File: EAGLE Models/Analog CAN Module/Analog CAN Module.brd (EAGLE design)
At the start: 98.3 x 80 mm, 230 parts, among them IC1 AT90CAN128, IC2 MCP2551SO8, IC3 NUP2105L, IC5 FT232RL, Q1 56P2859, U1 LTC2053, U10 LTC2053, U11 LTC2053, U12 LTC2053, U13 LTC2053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

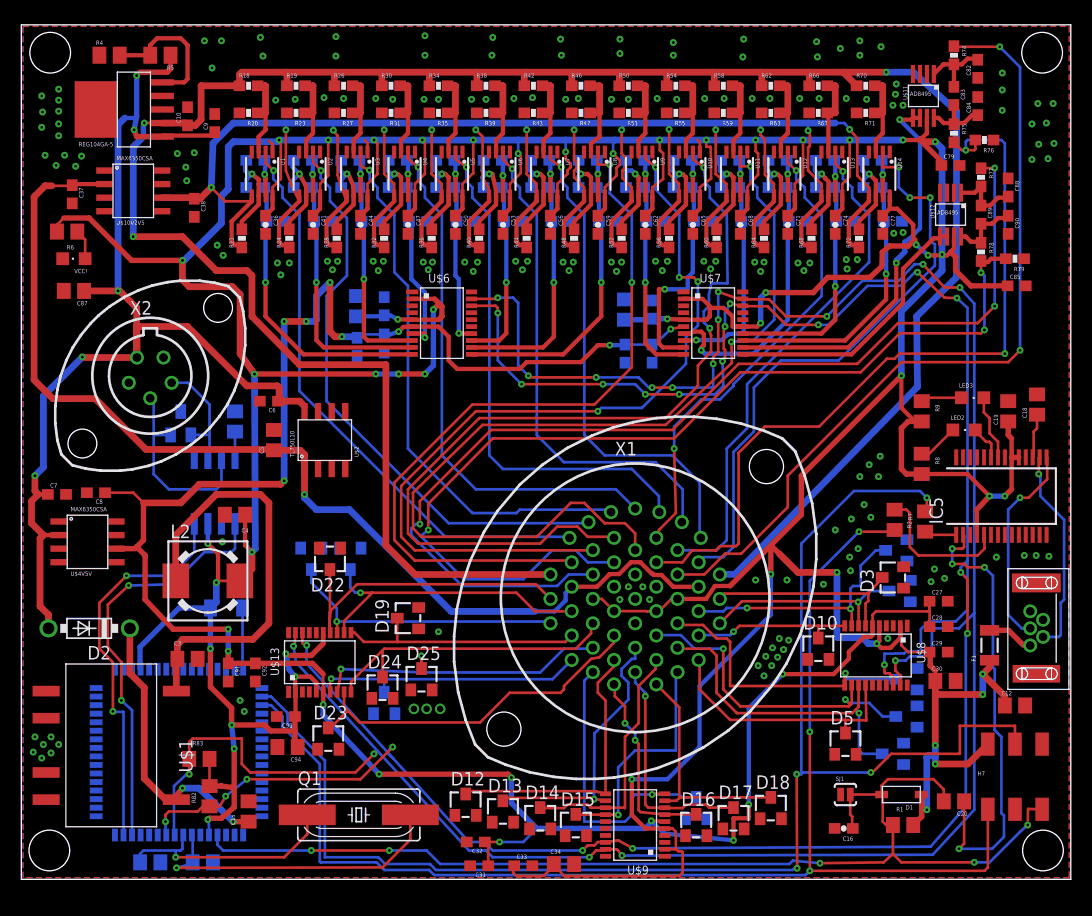
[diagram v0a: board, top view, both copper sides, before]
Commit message: Added USB connector and FTDI Chip, fixed feedback according to daniel, added PTC fuse, Added schottky diode for RVP and battery reverse bias
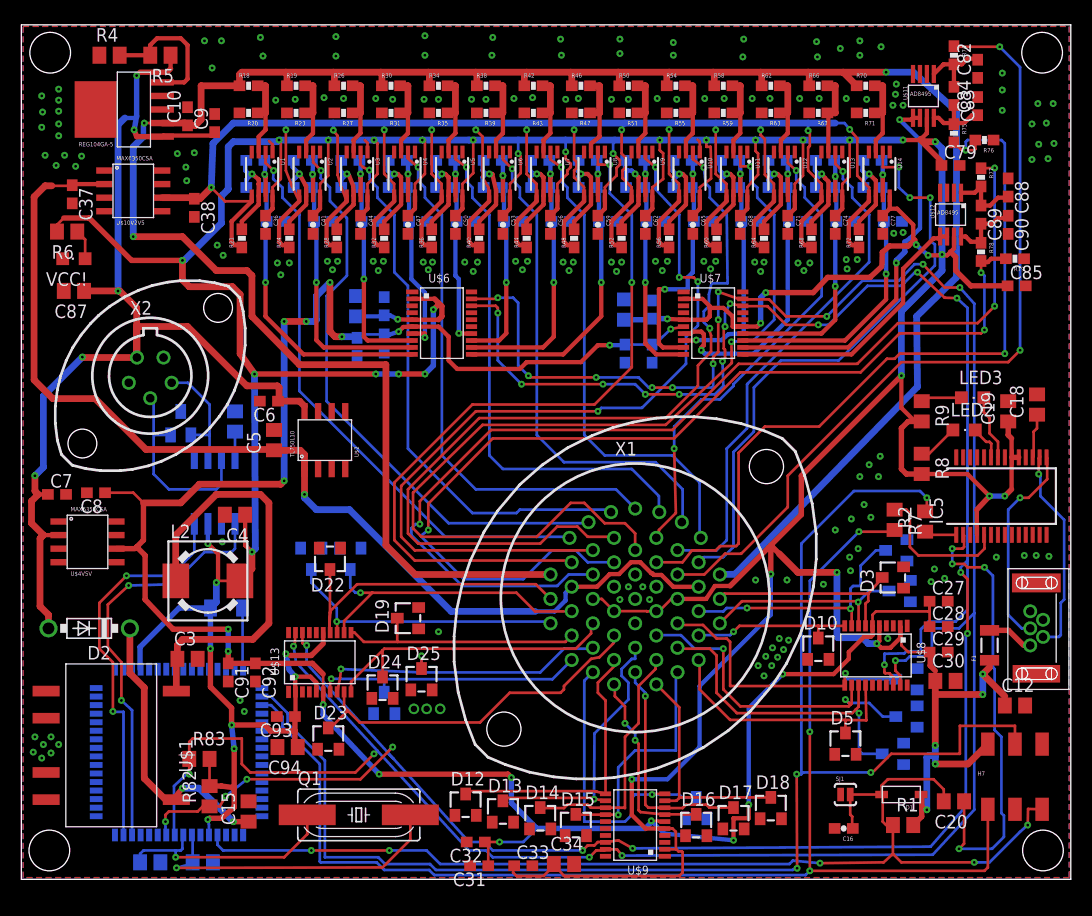
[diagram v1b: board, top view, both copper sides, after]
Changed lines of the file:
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@@
 <?xml version="1.0" encoding="utf-8"?>
 <!DOCTYPE eagle SYSTEM "eagle.dtd">
-<eagle version="7.4.0">
+<eagle version="7.7.0">
 <drawing>
 <settings>
@@
 <layers>
 <layer number="1" name="Top" color="4" fill="1" visible="yes" active="yes"/>
+<layer number="2" name="Route2" color="1" fill="3" visible="no" active="no"/>
+<layer number="3" name="Route3" color="4" fill="3" visible="no" active="no"/>
+<layer number="14" name="Route14" color="1" fill="6" visible="no" active="no"/>
+<layer number="15" name="Route15" color="4" fill="6" visible="no" active="no"/>
 <layer number="16" name="Bottom" color="1" fill="1" visible="yes" active="yes"/>
 <layer number="17" name="Pads" color="2" fill="1" visible="yes" active="yes"/>
